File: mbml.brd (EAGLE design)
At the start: 74.9 x 72.4 mm, 43 parts, among them K1 G5SB, K2 68800611622, Q1 2N2222, Q2 IRLZ24LPBF, U1 REG_5V_SWITCHING_SI-8050E, X1 43160-1102, X2 CON-2

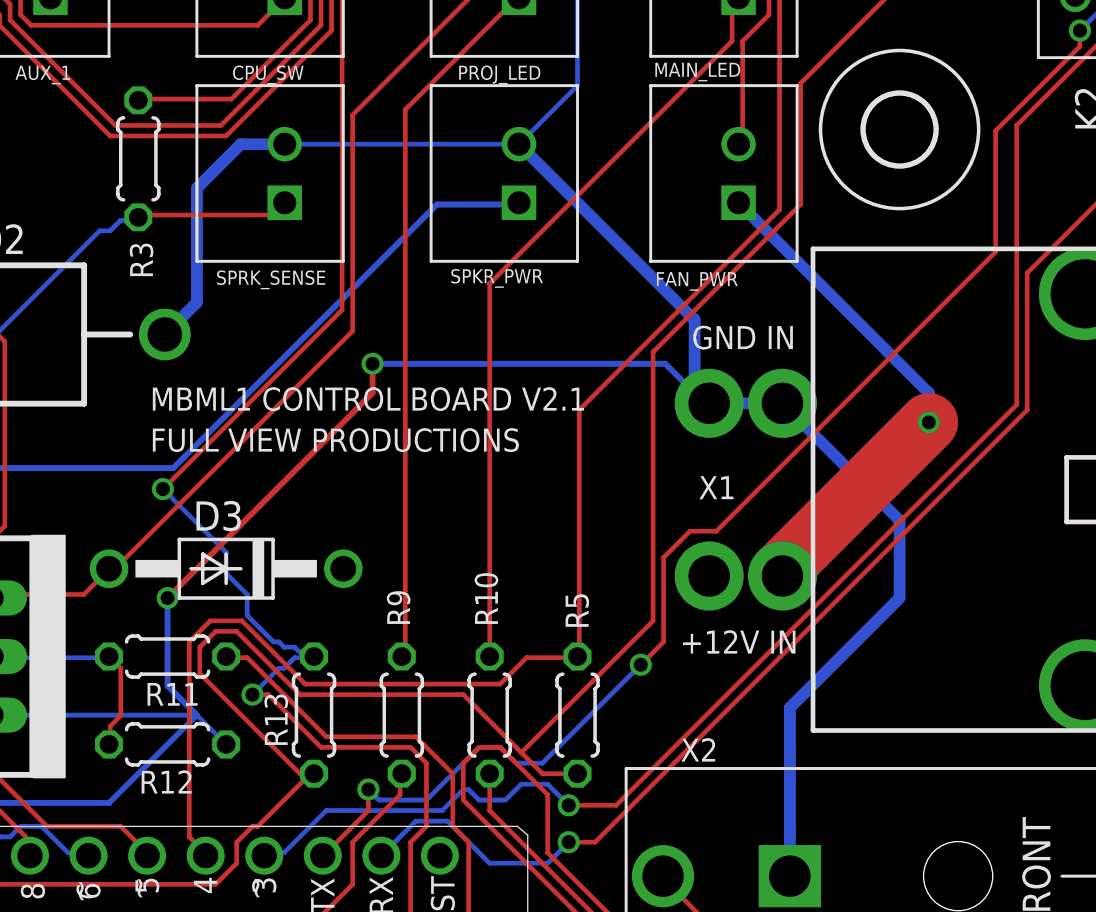
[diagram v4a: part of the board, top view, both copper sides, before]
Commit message: Added reverse polarity protection
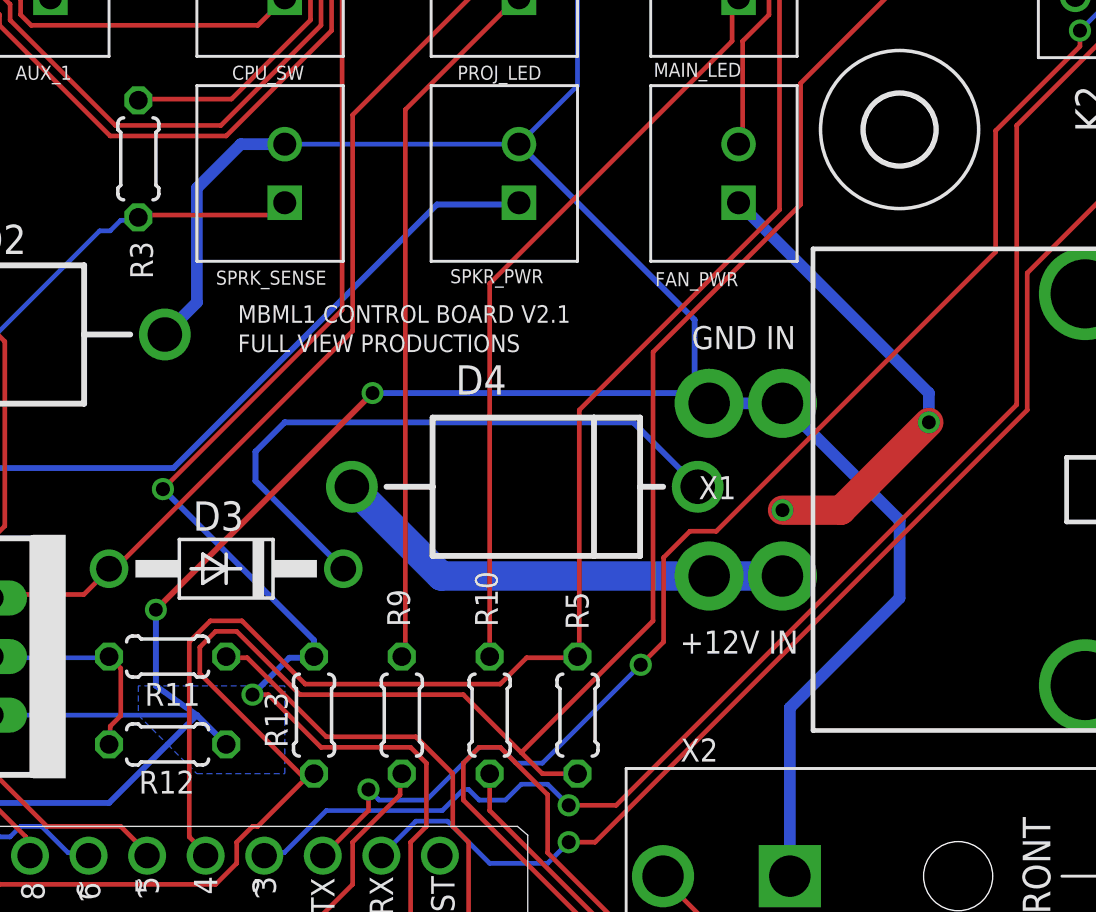
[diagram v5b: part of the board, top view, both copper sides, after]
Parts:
- added D4: (no value), TinkerTech:DO-201AD_AXIAL
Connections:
- new net +12V_IN: D4.+, X1.1@1
- net +12V: now also D4.-; no longer X1.1@1
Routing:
- net +12V: track 30.7 -> 56.9 mm, vias 2 -> 3
- net +12V_IN: track 0.00 -> 20.3 mm
- net GND: track 222.3 -> 221.1 mm
- net A3: track 83.1 -> 82.6 mm
- added copper zone on layer 16, net GND
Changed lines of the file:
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@@
 <text x="53.975" y="28.067" size="1" layer="25">+12V IN</text>
 <text x="68.072" y="13.462" size="1" layer="25" rot="R180">MONITOR PWR</text>
-<text x="30.988" y="36.83" size="1" layer="25" ratio="11">FULL VIEW PRODUCTIONS</text>
-<text x="30.988" y="38.608" size="1" layer="25" ratio="11">MBML1 CONTROL BOARD V2.1</text>
+<text x="34.798" y="41.148" size="0.762" layer="25" ratio="11">FULL VIEW PRODUCTIONS</text>
+<text x="34.798" y="42.418" size="0.762" layer="25" ratio="11">MBML1 CONTROL BOARD V2.1</text>
 <text x="55.626" y="24.384" size="1" layer="25" rot="R180">X2</text>
 <wire x1="74.676" y1="0.254" x2="0.254" y2="0.254" width="0.508" layer="40"/>
@@
 <attribute name="NAME" x="34.544" y="52.959" size="0.6096" layer="25"/>
 </element>
+<element name="D4" library="TinkerTech" package="DO-201AD_AXIAL" value="" x="47.244" y="35.306"/>
 </elements>
 <signals>
@@
 <wire x1="17.76" y1="25.4" x2="24.13" y2="25.4" width="0.2032" layer="16"/>
 <wire x1="24.13" y1="25.4" x2="33.02" y2="25.4" width="0.2032" layer="16"/>
-<wire x1="33.02" y1="25.4" x2="34.29" y2="24.13" width="0.2032" layer="16"/>
+<wire x1="33.02" y1="25.4" x2="34.29" y2="24.13" width="0.254" layer="16"/>
 <wire x1="46.99" y1="50.165" x2="36.83" y2="50.165" width="0.2032" layer="16"/>
 <wire x1="46.99" y1="59.055" x2="48.895" y2="59.055" width="0.2032" layer="16"/>
@@
 <wire x1="49.53" y1="52.705" x2="46.99" y2="50.165" width="0.2032" layer="16"/>
 <wire x1="58.42" y1="38.924" x2="55.056" y2="38.924" width="0.508" layer="16"/>
-<wire x1="55.056" y1="38.924" x2="54.61" y2="39.37" width="0.2032" layer="16"/>
-<wire x1="54.61" y1="39.37" x2="54.61" y2="42.545" width="0.508" layer="16"/>
-<wire x1="54.61" y1="42.545" x2="46.99" y2="50.165" width="0.508" layer="16"/>
+<wire x1="55.056" y1="38.924" x2="54.61" y2="39.37" width="0.254" layer="16"/>
+<wire x1="54.61" y1="39.37" x2="54.61" y2="42.545" width="0.254" layer="16"/>
+<wire x1="54.61" y1="42.545" x2="46.99" y2="50.165" width="0.254" layer="16"/>
 <wire x1="58.74" y1="18.415" x2="58.74" y2="25.72" width="0.508" layer="16"/>
 <wire x1="58.74" y1="25.72" x2="63.5" y2="30.48" width="0.508" layer="16"/>
@@
 <wire x1="19.05" y1="21.59" x2="19.05" y2="20.32" width="0.254" layer="16"/>
 <wire x1="19.05" y1="20.32" x2="17.78" y2="19.05" width="0.254" layer="16"/>
-<wire x1="33.02" y1="25.4" x2="31.75" y2="26.67" width="0.254" layer="16"/>
-<wire x1="31.75" y1="26.67" x2="31.75" y2="30.48" width="0.254" layer="16"/>
-<via x="31.75" y="30.48" extent="1-16" drill="0.6"/>
-<wire x1="31.75" y1="30.48" x2="40.64" y2="39.37" width="0.254" layer="1"/>
-<wire x1="40.64" y1="39.37" x2="40.64" y2="40.64" width="0.254" layer="1"/>
-<via x="40.64" y="40.64" extent="1-16" drill="0.6"/>
-<wire x1="40.64" y1="40.64" x2="53.34" y2="40.64" width="0.254" layer="16"/>
-<wire x1="53.34" y1="40.64" x2="54.61" y2="39.37" width="0.254" layer="16"/>
+<wire x1="33.02" y1="25.4" x2="31.242" y2="26.67" width="0.254" layer="16"/>
+<wire x1="31.242" y1="26.67" x2="31.242" y2="29.972" width="0.254" layer="16"/>
+<via x="31.242" y="29.972" extent="1-16" drill="0.6"/>
+<wire x1="31.242" y1="29.972" x2="40.64" y2="39.37" width="0.254" layer="1"/>
+<via x="40.64" y="39.37" extent="1-16" drill="0.6"/>
+<wire x1="40.64" y1="39.37" x2="54.61" y2="39.37" width="0.254" layer="16"/>
 <wire x1="71.12" y1="59.068" x2="71.107" y2="59.068" width="0.254" layer="16"/>
 <wire x1="71.107" y1="59.068" x2="64.77" y2="65.405" width="0.254" layer="16"/>
 <wire x1="64.77" y1="65.405" x2="56.515" y2="65.405" width="0.254" layer="16"/>
+<polygon width="0.254" layer="16">
+<vertex x="30.48" y="26.67"/>
+<vertex x="30.48" y="25.4"/>
+<vertex x="31.75" y="24.13"/>
+<vertex x="33.02" y="22.86"/>
+<vertex x="36.83" y="22.86"/>
+<vertex x="36.83" y="26.67"/>
+</polygon>
 </signal>
 <signal name="D3">
@@
 <contactref element="K1" pad="2"/>
 <contactref element="K1" pad="1"/>
-<contactref element="X1" pad="1@1"/>
 <contactref element="D1" pad="C"/>
 <contactref element="U$1" pad="BAT+"/>
@@
 <wire x1="15.5448" y1="19.431" x2="15.621" y2="19.304" width="0.2032" layer="16"/>
 <wire x1="15.5448" y1="19.6596" x2="15.6210125" y2="20.91750625" width="0.2032" layer="16"/>
-<wire x1="58.42" y1="31.434" x2="58.42" y2="31.75" width="0.508" layer="1"/>
-<wire x1="58.42" y1="31.75" x2="64.77" y2="38.1" width="2.54" layer="1"/>
 <via x="64.77" y="38.1" extent="1-16" drill="0.6"/>
 <wire x1="64.77" y1="38.1" x2="64.77" y2="39.37" width="0.508" layer="16"/>
@@
 <wire x1="15.26" y1="27.96" x2="16.51" y2="29.21" width="0.254" layer="1"/>
 <wire x1="16.51" y1="29.21" x2="19.05" y2="29.21" width="0.254" layer="1"/>
+<via x="58.42" y="34.29" extent="1-16" drill="0.6"/>
+<wire x1="58.42" y1="34.29" x2="60.96" y2="34.29" width="1.27" layer="1"/>
+<wire x1="60.96" y1="34.29" x2="64.77" y2="38.1" width="1.27" layer="1"/>
+<contactref element="D4" pad="-"/>
+<wire x1="39.37" y1="31.75" x2="35.56" y2="35.56" width="0.254" layer="16"/>
+<wire x1="35.56" y1="35.56" x2="35.56" y2="36.83" width="0.254" layer="16"/>
+<wire x1="35.56" y1="36.83" x2="36.83" y2="38.1" width="0.254" layer="16"/>
+<wire x1="54.744" y1="35.306" x2="51.95" y2="38.1" width="0.254" layer="16"/>
+<wire x1="51.95" y1="38.1" x2="36.83" y2="38.1" width="0.254" layer="16"/>
 </signal>
 <signal name="MON_PWR">
@@
 <contactref element="R13" pad="1"/>
 <contactref element="PROJ_BLANK" pad="P$2"/>
-<wire x1="37.2618" y1="27.8892" x2="37.719" y2="27.8892" width="0.2032" layer="16"/>
-<wire x1="37.719" y1="27.8892" x2="37.9476" y2="27.8892" width="0.2032" layer="16"/>
-<wire x1="36.8046" y1="27.432" x2="37.2618" y2="27.8892" width="0.2032" layer="16"/>
-<wire x1="36.576" y1="27.432" x2="36.8046" y2="27.432" width="0.2032" layer="16"/>
-<wire x1="35.433" y1="26.289" x2="36.576" y2="27.432" width="0.2032" layer="16"/>
 <wire x1="36.1188" y1="26.289" x2="35.433" y2="26.289" width="0.2032" layer="1"/>
 <wire x1="38.4048" y1="24.003" x2="36.1188" y2="26.289" width="0.2032" layer="1"/>
@@
 <wire x1="39.3192" y1="42.9768" x2="39.3192" y2="59.8932" width="0.2032" layer="1"/>
 <wire x1="31.5468" y1="35.2044" x2="39.3192" y2="42.9768" width="0.2032" layer="1"/>
-<wire x1="34.29" y1="32.4612" x2="31.5468" y2="35.2044" width="0.2032" layer="16"/>
-<wire x1="34.29" y1="31.5468" x2="34.29" y2="32.4612" width="0.2032" layer="16"/>
-<wire x1="35.2044" y1="30.6324" x2="34.29" y2="31.5468" width="0.2032" layer="16"/>
-<wire x1="35.2044" y1="29.718" x2="35.2044" y2="30.6324" width="0.2032" layer="16"/>
-<wire x1="36.3474" y1="28.575" x2="35.2044" y2="29.718" width="0.2032" layer="16"/>
-<wire x1="36.576" y1="28.575" x2="36.3474" y2="28.575" width="0.2032" layer="16"/>
-<wire x1="36.8046" y1="28.3464" x2="36.576" y2="28.575" width="0.2032" layer="16"/>
-<wire x1="37.2618" y1="28.3464" x2="36.8046" y2="28.3464" width="0.2032" layer="16"/>
-<wire x1="37.719" y1="27.8892" x2="37.2618" y2="28.3464" width="0.2032" layer="16"/>
 <wire x1="46.863" y1="67.8942" x2="46.99" y2="67.945" width="0.2032" layer="1"/>
 <wire x1="37.719" y1="27.8892" x2="38.1" y2="27.94" width="0.2032" layer="16"/>
 <via x="35.433" y="26.289" extent="1-16" drill="0.6096"/>
 <via x="31.5468" y="35.2044" extent="1-16" drill="0.6096"/>
+<wire x1="37.719" y1="27.8892" x2="37.0332" y2="27.8892" width="0.254" layer="16"/>
+<wire x1="37.0332" y1="27.8892" x2="35.433" y2="26.289" width="0.254" layer="16"/>
+<wire x1="31.5468" y1="35.2044" x2="38.1" y2="28.6512" width="0.254" layer="16"/>
+<wire x1="38.1" y1="28.6512" x2="38.1" y2="27.94" width="0.254" layer="16"/>
 </signal>
 <signal name="A4">
@@
 <wire x1="36.8046" y1="56.4642" x2="36.83" y2="56.515" width="0.2032" layer="1"/>
 </signal>
+<signal name="+12V_IN">
+<contactref element="D4" pad="+"/>
+<contactref element="X1" pad="1@1"/>
+<wire x1="58.42" y1="31.434" x2="43.616" y2="31.434" width="1.27" layer="16"/>
+<wire x1="43.616" y1="31.434" x2="39.744" y2="35.306" width="1.27" layer="16"/>
+</signal>
 </signals>
